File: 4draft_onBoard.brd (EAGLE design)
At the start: 88.6 x 88.9 mm, 68 parts, among them IC3 74ABT125PW, IC4 MAX4466KS, J2 USB_MINI-B_DIGIKEY, Q1 NPN 40V 1A SOT-23

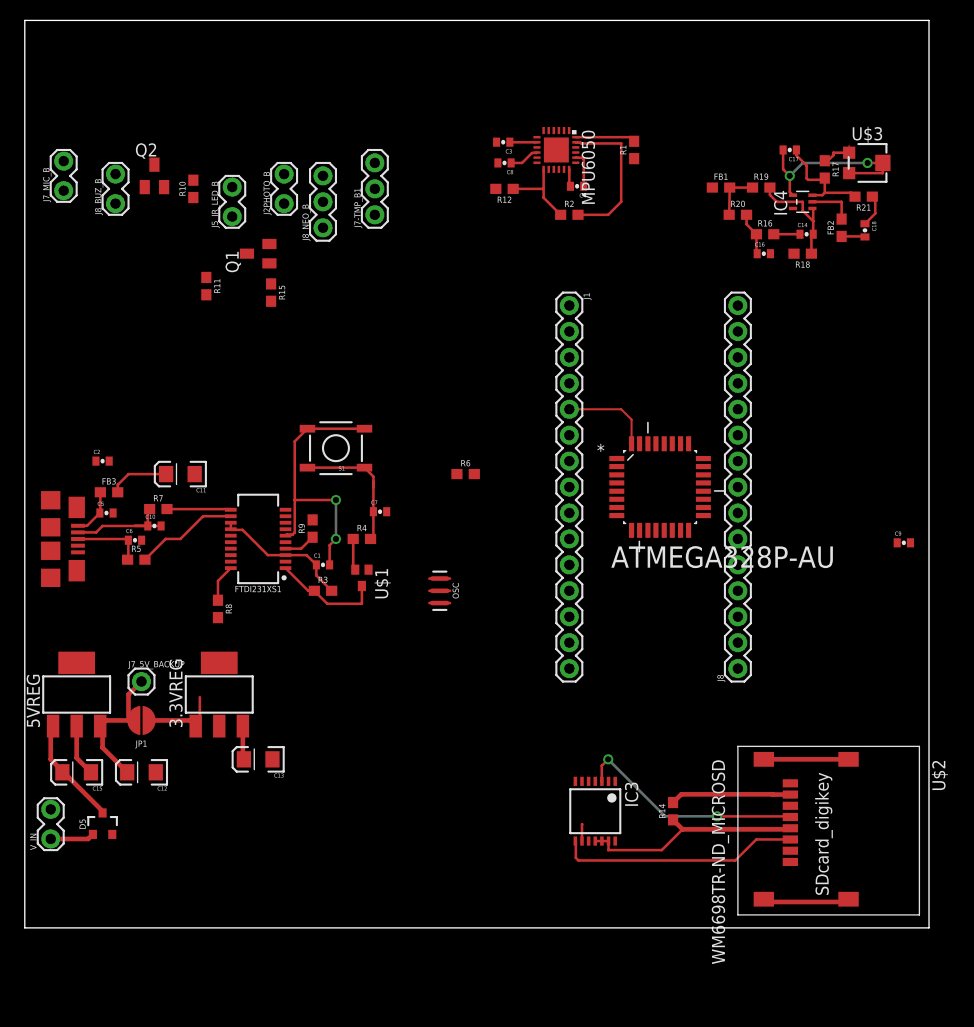
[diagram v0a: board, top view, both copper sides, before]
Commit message: shrinking board llayout
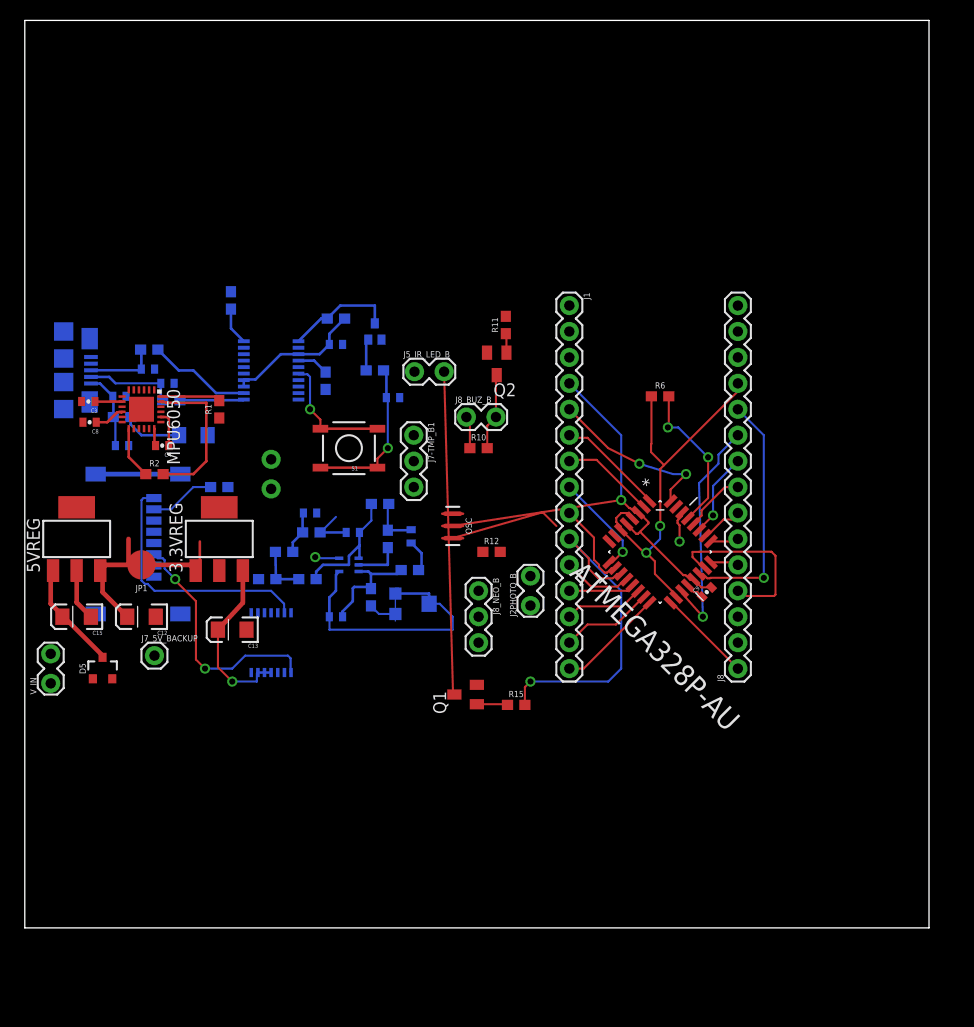
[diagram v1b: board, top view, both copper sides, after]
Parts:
- moved C17 63.8 mm to (30.5, 30.5), flipped to the bottom, turned to 0 degrees
- moved U$2 63.6 mm to (15.2, 44.5), flipped to the bottom
- moved U$3 62.0 mm to (38.1, 31.8), flipped to the bottom, turned to 180 degrees
- moved R17 61.1 mm to (33.9, 32.4), flipped to the bottom, turned to 90 degrees
- moved FB1 58.7 mm to (23.7, 34.2), flipped to the bottom, turned to 180 degrees
- moved R19 58.7 mm to (27.7, 34.2), flipped to the bottom, turned to 180 degrees
- moved R21 57.6 mm to (37.7, 35.1), flipped to the bottom, turned to 0 degrees
- moved IC4 56.9 mm to (31.8, 35.6), flipped to the bottom, turned to 270 degrees
- moved R20 55.4 mm to (25.4, 36.8), flipped to the bottom, turned to 180 degrees
- moved R14 54.6 mm to (19.1, 43.2), flipped to the bottom, turned to 0 degrees
- moved FB2 53.9 mm to (35.6, 38.1), flipped to the bottom, turned to 270 degrees
- moved C18 53.6 mm to (37.8, 38.4), flipped to the bottom, turned to 90 degrees
- moved C14 53.2 mm to (32.1, 38.7), flipped to the bottom, turned to 180 degrees
- moved R16 53.2 mm to (28.1, 38.7), flipped to the bottom, turned to 180 degrees
- moved C16 51.2 mm to (27.9, 40.6), flipped to the bottom, turned to 180 degrees
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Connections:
- net GND: no longer J8.14, J8.2
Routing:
- net 5V: track 23.2 -> 63.0 mm, vias 0 -> 2
- net D7: track 0.00 -> 34.1 mm, vias 0 -> 1
- net IR_-: track 0.00 -> 31.9 mm
- net A6: track 0.00 -> 25.0 mm, vias 0 -> 2
- net N$10: track 0.00 -> 25.0 mm
- net A7: track 0.00 -> 24.1 mm, vias 0 -> 1
- net SCK_BUFF: track 22.7 -> 0.00 mm, vias 2 -> 0
- net GND: track 61.5 -> 83.1 mm
- net A0: track 0.00 -> 18.3 mm
- net RESET: track 0.00 -> 15.0 mm, vias 0 -> 2
- net N$2: track 0.00 -> 11.1 mm
- net D3: track 0.00 -> 10.8 mm
- net D5: track 0.00 -> 10.3 mm, vias 0 -> 1
- net SCK: track 0.00 -> 9.27 mm
- net D4: track 0.00 -> 9.27 mm
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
